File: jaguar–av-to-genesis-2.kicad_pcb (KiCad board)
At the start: 2 copper layers, 30.5 x 24.4 mm, 4 parts, among them J1 JaguarAV_24, J2 Genesis2AV

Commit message: Small fixes
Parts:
- added G***: LOGO, logos:leaded-solder-logo-800dpi, F.Cu at (147.8, 81.7)

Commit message: add this side down warning
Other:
- board text added: "this side down!"
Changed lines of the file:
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@@
   (general
     (thickness 1.6)
-    (drawings 13)
+    (drawings 14)
     (tracks 74)
     (zones 0)
@@
       ))
   )
+  (gr_text "this side down!" (at 148.209 84.836) (layer B.SilkS)
+    (effects (font (size 1 1) (thickness 0.15)) (justify mirror))
+  )
   (gr_text "Aud. R" (at 150.622 80.518 45) (layer B.SilkS)
     (effects (font (size 0.75 0.75) (thickness 0.15)) (justify mirror))
@@
   (gr_line (start 132.842 94.742) (end 132.842 70.358) (layer Edge.Cuts) (width 0.05))
   (gr_line (start 163.322 94.742) (end 132.842 94.742) (layer Edge.Cuts) (width 0.05))
-  (segment (start 136.779 82.931) (end 138.176 81.534) (width 0.25) (layer B.Cu) (net 16))
-  (via (at 138.176 81.534) (size 0.8) (drill 0.4) (layers F.Cu B.Cu) (net 16))
-  (segment (start 136.779 90.424) (end 136.779 82.931) (width 0.25) (layer B.Cu) (net 16) (status 10))
-  (segment (start 138.176 81.534) (end 144.272 81.534) (width 0.25) (layer F.Cu) (net 16))
-  (segment (start 146.436 79.37) (end 146.436 78.002) (width 0.25) (layer F.Cu) (net 16) (status 20))
-  (segment (start 144.272 81.534) (end 146.436 79.37) (width 0.25) (layer F.Cu) (net 16))
   (segment (start 142.778 71.852) (end 148.336 71.852) (width 0.5) (layer B.Cu) (net 2) (status 20))
   (segment (start 139.319 75.311) (end 142.778 71.852) (width 0.5) (layer B.Cu) (net 2))
@@
   (segment (start 159.639 87.503) (end 159.639 90.424) (width 0.5) (layer F.Cu) (net 2) (status 30))
   (via (at 159.639 87.503) (size 0.8) (drill 0.4) (layers F.Cu B.Cu) (net 2) (status 30))
+  (segment (start 162.179 90.424) (end 162.179 83.947) (width 0.25) (layer B.Cu) (net 6) (status 10))
+  (via (at 160.782 82.55) (size 0.8) (drill 0.4) (layers F.Cu B.Cu) (net 6))
+  (segment (start 162.179 83.947) (end 160.782 82.55) (width 0.25) (layer B.Cu) (net 6))
+  (segment (start 156.234 78.002) (end 152.186 78.002) (width 0.25) (layer F.Cu) (net 6) (status 20))
+  (segment (start 160.782 82.55) (end 156.234 78.002) (width 0.25) (layer F.Cu) (net 6))
+  (segment (start 150.236 77.152) (end 150.236 78.002) (width 0.25) (layer B.Cu) (net 14) (status 20))
+  (segment (start 152.186 75.202) (end 150.236 77.152) (width 0.25) (layer B.Cu) (net 14) (status 10))
+  (segment (start 162.179 86.654) (end 155.194 79.669) (width 0.25) (layer F.Cu) (net 14) (status 10))
+  (segment (start 162.179 90.424) (end 162.179 86.654) (width 0.25) (layer F.Cu) (net 14) (status 30))
+  (segment (start 151.903 79.669) (end 150.236 78.002) (width 0.25) (layer F.Cu) (net 14) (status 20))
+  (segment (start 155.194 79.669) (end 151.903 79.669) (width 0.25) (layer F.Cu) (net 14))
+  (segment (start 136.779 82.931) (end 138.176 81.534) (width 0.25) (layer B.Cu) (net 16))
+  (via (at 138.176 81.534) (size 0.8) (drill 0.4) (layers F.Cu B.Cu) (net 16))
+  (segment (start 136.779 90.424) (end 136.779 82.931) (width 0.25) (layer B.Cu) (net 16) (status 10))
+  (segment (start 138.176 81.534) (end 144.272 81.534) (width 0.25) (layer F.Cu) (net 16))
+  (segment (start 146.436 79.37) (end 146.436 78.002) (width 0.25) (layer F.Cu) (net 16) (status 20))
+  (segment (start 144.272 81.534) (end 146.436 79.37) (width 0.25) (layer F.Cu) (net 16))
   (segment (start 152.019 86.654) (end 148.336 82.971) (width 0.25) (layer B.Cu) (net 17) (status 10))
   (segment (start 152.019 90.424) (end 152.019 86.654) (width 0.25) (layer B.Cu) (net 17) (status 30))
@@
   (segment (start 144.486 78.446) (end 144.486 78.002) (width 0.25) (layer B.Cu) (net 18) (status 30))
   (segment (start 146.812 80.772) (end 144.486 78.446) (width 0.25) (layer B.Cu) (net 18) (status 20))
-  (segment (start 162.179 90.424) (end 162.179 83.947) (width 0.25) (layer B.Cu) (net 6) (status 10))
-  (via (at 160.782 82.55) (size 0.8) (drill 0.4) (layers F.Cu B.Cu) (net 6))
-  (segment (start 162.179 83.947) (end 160.782 82.55) (width 0.25) (layer B.Cu) (net 6))
-  (segment (start 156.234 78.002) (end 152.186 78.002) (width 0.25) (layer F.Cu) (net 6) (status 20))
-  (segment (start 160.782 82.55) (end 156.234 78.002) (width 0.25) (layer F.Cu) (net 6))
   (segment (start 144.486 75.202) (end 143.256 76.432) (width 0.25) (layer B.Cu) (net 19) (status 10))
   (via (at 146.304 84.582) (size 0.8) (drill 0.4) (layers F.Cu B.Cu) (net 19))
@@
   (segment (start 152.146 90.297) (end 152.019 90.424) (width 0.25) (layer F.Cu) (net 20) (status 30))
   (segment (start 152.146 85.09) (end 152.146 90.297) (width 0.25) (layer F.Cu) (net 20) (status 20))
-  (segment (start 150.236 77.152) (end 150.236 78.002) (width 0.25) (layer B.Cu) (net 14) (status 20))
-  (segment (start 152.186 75.202) (end 150.236 77.152) (width 0.25) (layer B.Cu) (net 14) (status 10))
-  (segment (start 162.179 86.654) (end 155.194 79.669) (width 0.25) (layer F.Cu) (net 14) (status 10))
-  (segment (start 162.179 90.424) (end 162.179 86.654) (width 0.25) (layer F.Cu) (net 14) (status 30))
-  (segment (start 151.903 79.669) (end 150.236 78.002) (width 0.25) (layer F.Cu) (net 14) (status 20))
-  (segment (start 155.194 79.669) (end 151.903 79.669) (width 0.25) (layer F.Cu) (net 14))
   (segment (start 147.374 73.66) (end 146.836 74.198) (width 0.25) (layer B.Cu) (net 20))
   (segment (start 152.146 82.55) (end 154.286001 80.409999) (width 0.25) (layer B.Cu) (net 20))

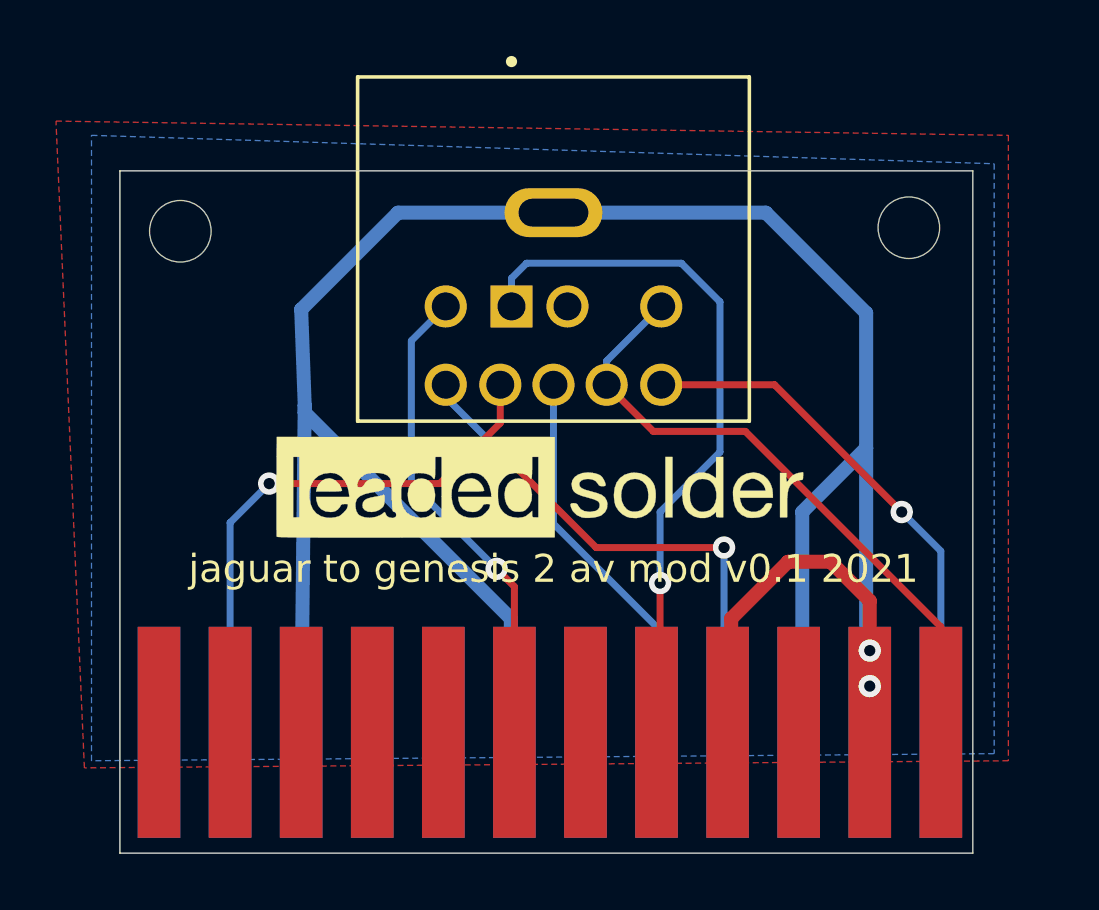
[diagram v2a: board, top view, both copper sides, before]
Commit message: Pin callouts
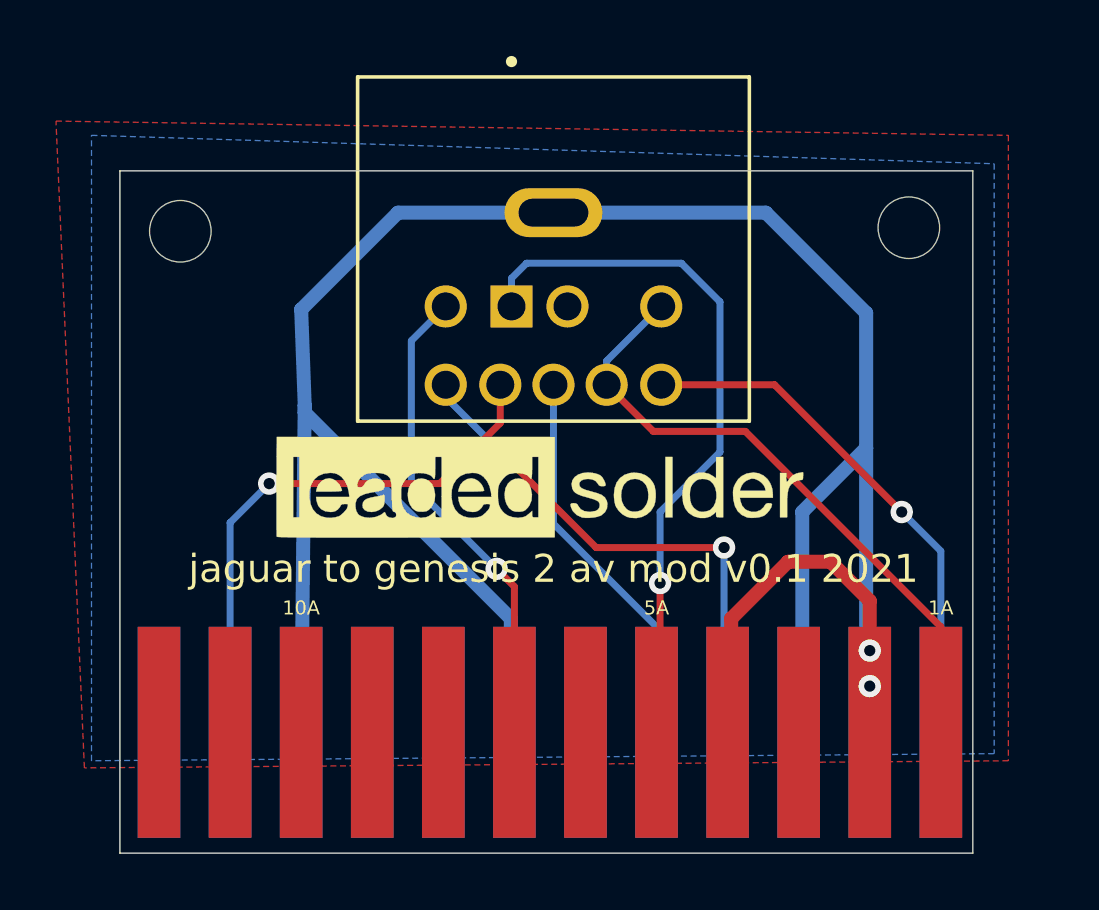
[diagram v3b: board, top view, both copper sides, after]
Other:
- board text added: "10A"
- board text added: "10B"
- board text added: "1A"
- board text added: "1B"
- board text added: "5A"
- board text added: "5B"
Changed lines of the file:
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@@
   (general
     (thickness 1.6)
-    (drawings 14)
+    (drawings 20)
     (tracks 74)
     (zones 0)
@@
       ))
   )
+  (gr_text 10B (at 139.319 85.979) (layer B.SilkS)
+    (effects (font (size 0.5 0.5) (thickness 0.125)) (justify mirror))
+  )
+  (gr_text 5B (at 152.019 85.979) (layer B.SilkS)
+    (effects (font (size 0.5 0.5) (thickness 0.125)) (justify mirror))
+  )
+  (gr_text 1B (at 162.179 85.979) (layer B.SilkS)
+    (effects (font (size 0.5 0.5) (thickness 0.125)) (justify mirror))
+  )
+  (gr_text 10A (at 139.319 85.979) (layer F.SilkS)
+    (effects (font (size 0.5 0.5) (thickness 0.125)))
+  )
+  (gr_text 5A (at 152.019 85.979) (layer F.SilkS)
+    (effects (font (size 0.5 0.5) (thickness 0.125)))
+  )
+  (gr_text 1A (at 162.179 85.979) (layer F.SilkS)
+    (effects (font (size 0.5 0.5) (thickness 0.125)))
+  )
   (gr_text "this side down!" (at 148.209 84.836) (layer B.SilkS)
